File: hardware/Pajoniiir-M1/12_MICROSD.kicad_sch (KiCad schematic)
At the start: 23 parts

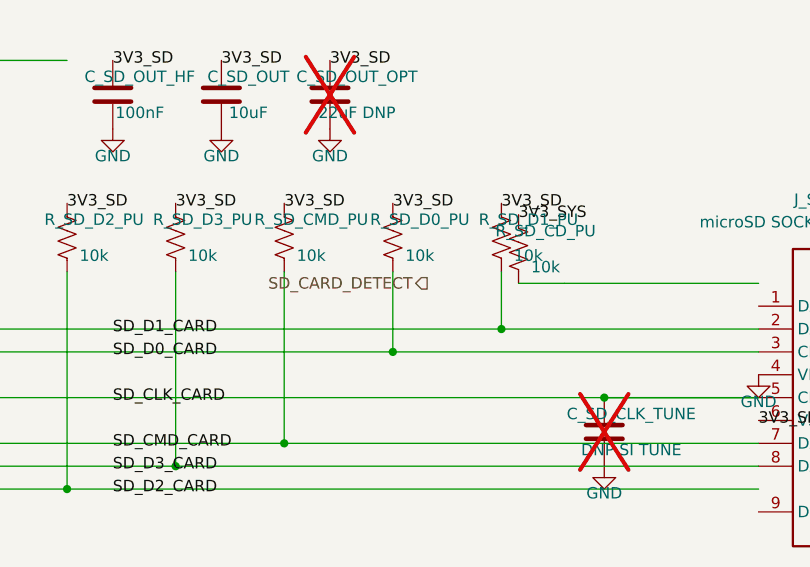
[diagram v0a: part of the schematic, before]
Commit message: hardware: bind remaining hierarchical ports to nets
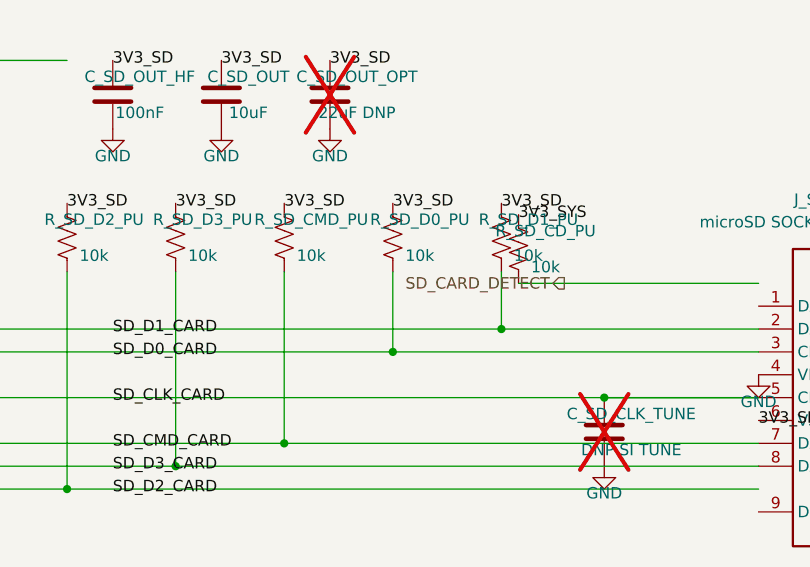
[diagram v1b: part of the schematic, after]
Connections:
- net SD_CARD_DETECT: now also R_SD_CD_PU.2
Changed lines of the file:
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@@
   )
   (wire (pts (xy 196.85 72.39) (xy 175.26 72.39)) (stroke (width 0) (type default)))
-  (hierarchical_label "SD_CARD_DETECT" (shape output) (at 160.02 72.39 180) (effects (font (size 1.27 1.27))))
+  (hierarchical_label "SD_CARD_DETECT" (shape output) (at 175.26 72.39 180) (effects (font (size 1.27 1.27))))
   (symbol
     (lib_id "Device:R_US") (at 170.18 68.58 0) (unit 1)

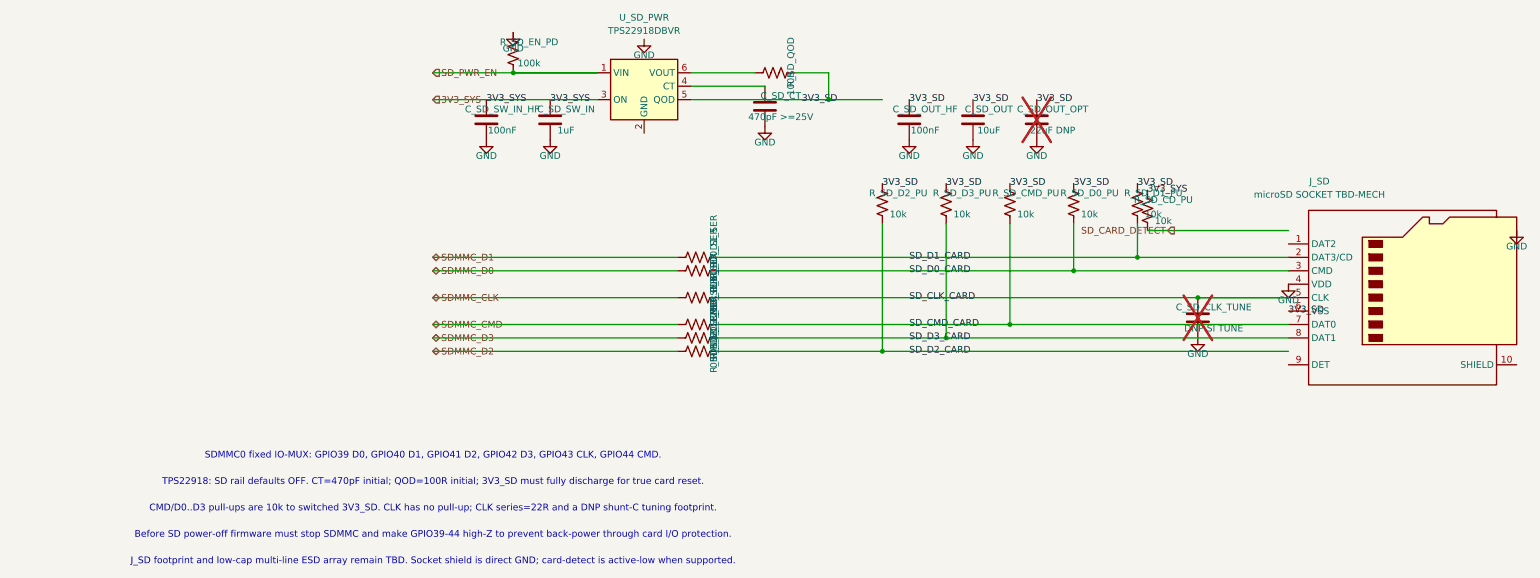
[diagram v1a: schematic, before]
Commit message: hardware: correct microSD power and signal mapping
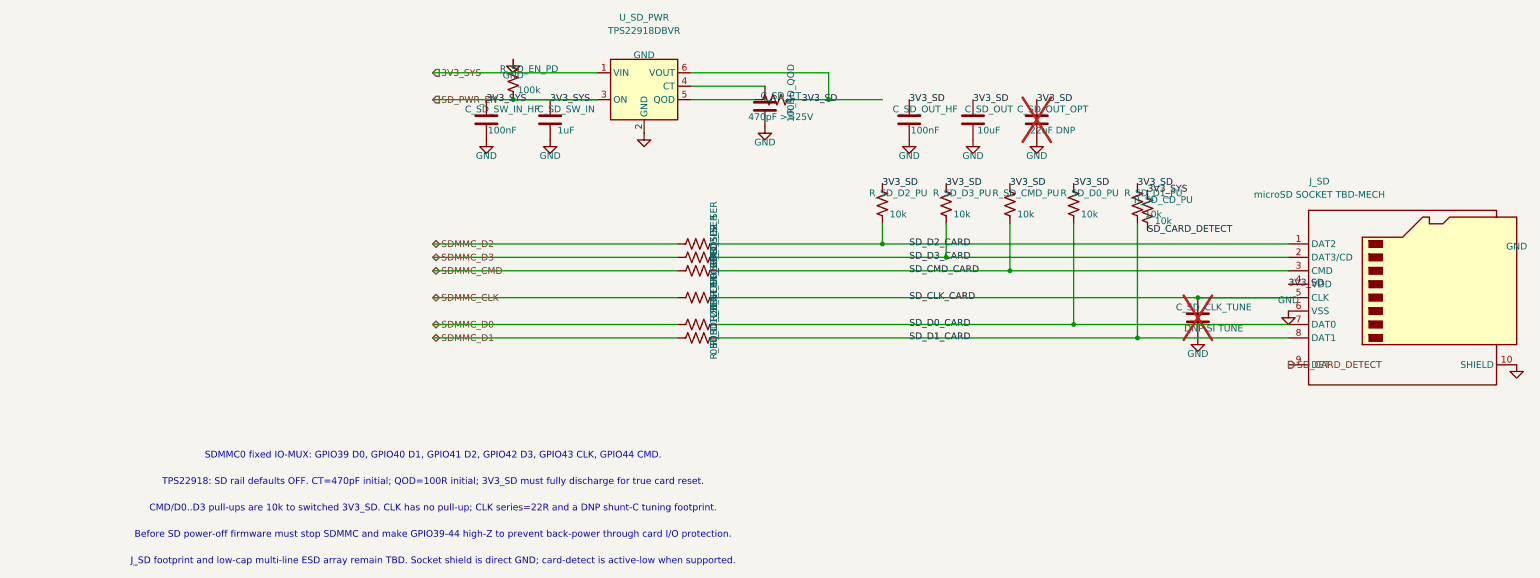
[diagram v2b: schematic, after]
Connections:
- net SD_PWR_EN is gone; now on net 3V3_SYS: R_SD_EN_PD.2, U_SD_PWR.1 (VIN)
- net 3V3_SD: now also J_SD.4 (VDD), U_SD_PWR.6 (VOUT); no longer J_SD.6 (VSS), U_SD_PWR.5 (QOD)
- net GND: now also J_SD.10 (SHIELD), J_SD.6 (VSS), U_SD_PWR.2 (GND); no longer J_SD.4 (VDD)
- net SD_CARD_DETECT: now also J_SD.9 (DET)
- net SD_CMD_CARD: now also J_SD.3 (CMD); no longer J_SD.7 (DAT0)
- net SD_D0_CARD: now also J_SD.7 (DAT0); no longer J_SD.3 (CMD)
- net SD_D1_CARD: now also J_SD.8 (DAT1); no longer J_SD.2 (DAT3/CD)
- net SD_D2_CARD: now also J_SD.1 (DAT2)
- net SD_D3_CARD: now also J_SD.2 (DAT3/CD); no longer J_SD.8 (DAT1)
- net at R_SD_QOD.1: now also U_SD_PWR.5 (QOD); no longer U_SD_PWR.6 (VOUT)
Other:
- moved on the sheet: R_SD_CMD_SER, R_SD_D0_SER, R_SD_D1_SER, R_SD_D2_SER, R_SD_D3_SER, R_SD_EN_PD, R_SD_QOD

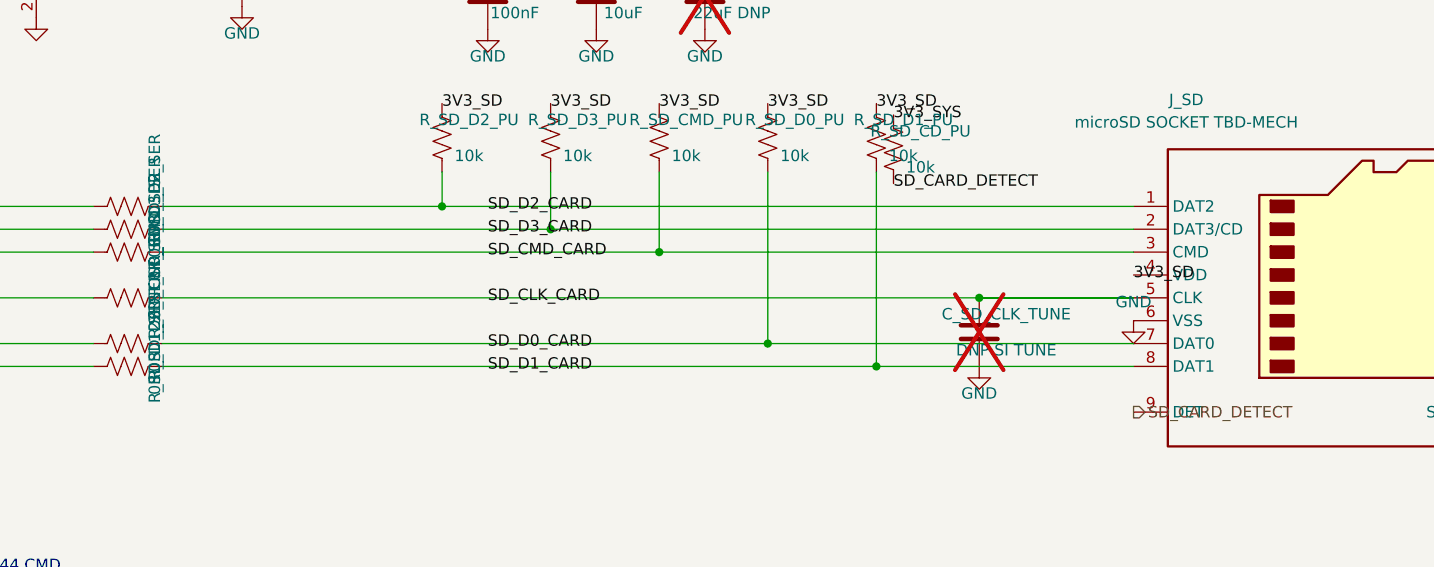
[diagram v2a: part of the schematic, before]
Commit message: hardware: close peripheral endpoint and net-alias gaps
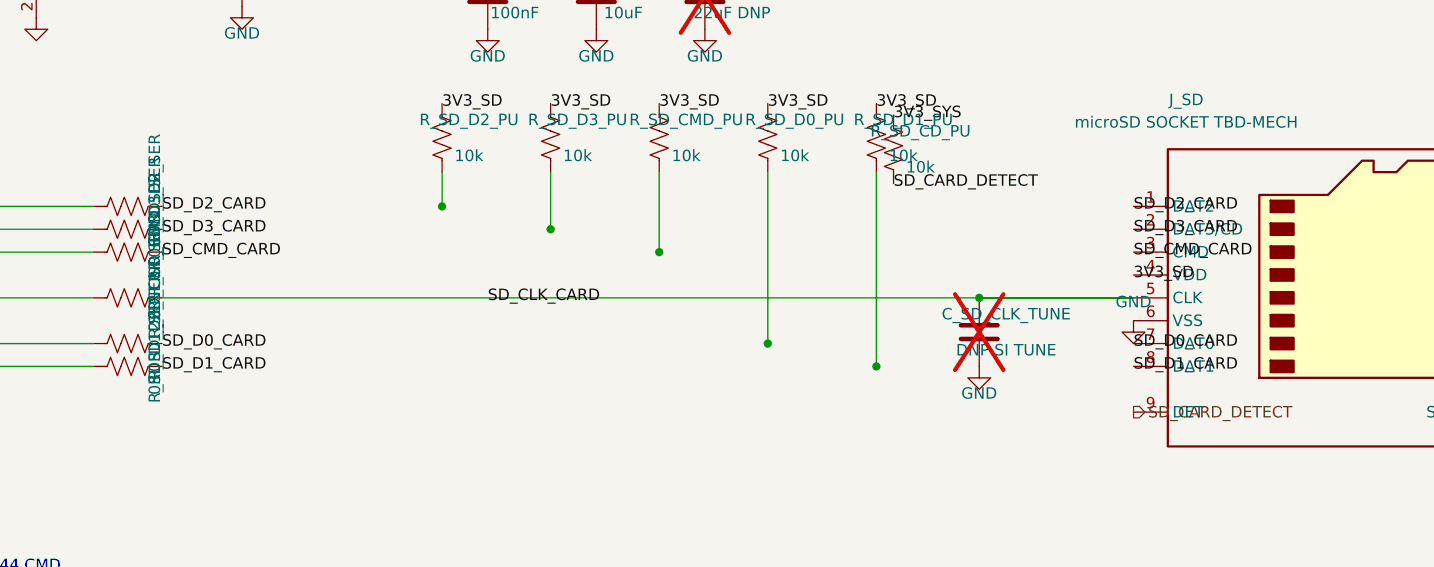
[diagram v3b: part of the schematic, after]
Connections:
- net SD_CMD_CARD: no longer R_SD_CMD_PU.2
- net SD_D0_CARD: no longer R_SD_D0_PU.2
- net SD_D1_CARD: no longer R_SD_D1_PU.2
- net SD_D2_CARD: no longer R_SD_D2_PU.2
- net SD_D3_CARD: no longer R_SD_D3_PU.2
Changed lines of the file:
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@@
     (comment 2 "Socket footprint and optional low-C ESD remain TBD-MECH/TBD-ESD")
   )
+  (label "SD_D2_CARD" (at 196.85 74.93 0) (effects (font (size 1.27 1.27))))
+  (label "SD_D3_CARD" (at 196.85 77.47 0) (effects (font (size 1.27 1.27))))
+  (label "SD_CMD_CARD" (at 196.85 80.01 0) (effects (font (size 1.27 1.27))))
+  (label "SD_D0_CARD" (at 196.85 90.17 0) (effects (font (size 1.27 1.27))))
+  (label "SD_D1_CARD" (at 196.85 92.71 0) (effects (font (size 1.27 1.27))))
   (label "SD_CARD_DETECT" (at 170.18 72.39 0) (effects (font (size 1.27 1.27))))
   (wire (pts (xy 83.82 42.545) (xy 109.855 42.545)) (stroke (width 0) (type default)))
@@
   )
   (wire (pts (xy 34.925 74.93) (xy 81.28 74.93)) (stroke (width 0) (type default)))
-  (wire (pts (xy 88.9 74.93) (xy 196.85 74.93)) (stroke (width 0) (type default)))
-  (label "SD_D2_CARD" (at 125.095 74.93 0) (effects (font (size 1.27 1.27))))
+  (label "SD_D2_CARD" (at 88.9 74.93 0) (effects (font (size 1.27 1.27))))
   (hierarchical_label "SDMMC_D3" (shape bidirectional) (at 34.925 77.47 0) (effects (font (size 1.27 1.27))))
   (symbol
@@
   )
   (wire (pts (xy 34.925 77.47) (xy 81.28 77.47)) (stroke (width 0) (type default)))
-  (wire (pts (xy 88.9 77.47) (xy 196.85 77.47)) (stroke (width 0) (type default)))
-  (label "SD_D3_CARD" (at 125.095 77.47 0) (effects (font (size 1.27 1.27))))
+  (label "SD_D3_CARD" (at 88.9 77.47 0) (effects (font (size 1.27 1.27))))
   (hierarchical_label "SDMMC_CMD" (shape bidirectional) (at 34.925 80.01 0) (effects (font (size 1.27 1.27))))
   (symbol
@@
   )
   (wire (pts (xy 34.925 80.01) (xy 81.28 80.01)) (stroke (width 0) (type default)))
-  (wire (pts (xy 88.9 80.01) (xy 196.85 80.01)) (stroke (width 0) (type default)))
-  (label "SD_CMD_CARD" (at 125.095 80.01 0) (effects (font (size 1.27 1.27))))
+  (label "SD_CMD_CARD" (at 88.9 80.01 0) (effects (font (size 1.27 1.27))))
   (hierarchical_label "SDMMC_CLK" (shape bidirectional) (at 34.925 85.09 0) (effects (font (size 1.27 1.27))))
   (symbol
@@
   )
   (wire (pts (xy 34.925 90.17) (xy 81.28 90.17)) (stroke (width 0) (type default)))
-  (wire (pts (xy 88.9 90.17) (xy 196.85 90.17)) (stroke (width 0) (type default)))
-  (label "SD_D0_CARD" (at 125.095 90.17 0) (effects (font (size 1.27 1.27))))
+  (label "SD_D0_CARD" (at 88.9 90.17 0) (effects (font (size 1.27 1.27))))
   (hierarchical_label "SDMMC_D1" (shape bidirectional) (at 34.925 92.71 0) (effects (font (size 1.27 1.27))))
   (symbol
@@
   )
   (wire (pts (xy 34.925 92.71) (xy 81.28 92.71)) (stroke (width 0) (type default)))
-  (wire (pts (xy 88.9 92.71) (xy 196.85 92.71)) (stroke (width 0) (type default)))
-  (label "SD_D1_CARD" (at 125.095 92.71 0) (effects (font (size 1.27 1.27))))
+  (label "SD_D1_CARD" (at 88.9 92.71 0) (effects (font (size 1.27 1.27))))
   (symbol
     (lib_id "Device:R_US") (at 120.015 67.31 0) (unit 1)

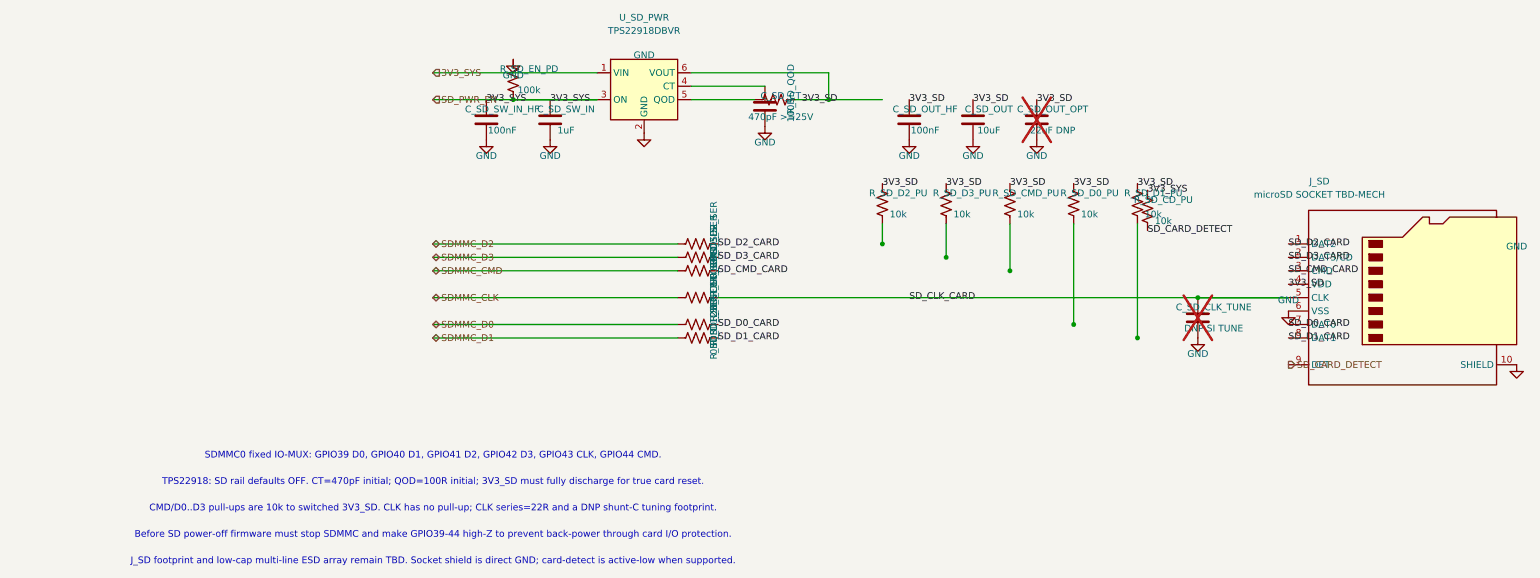
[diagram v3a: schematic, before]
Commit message: hardware: normalize endpoint nets and fix microSD input rail
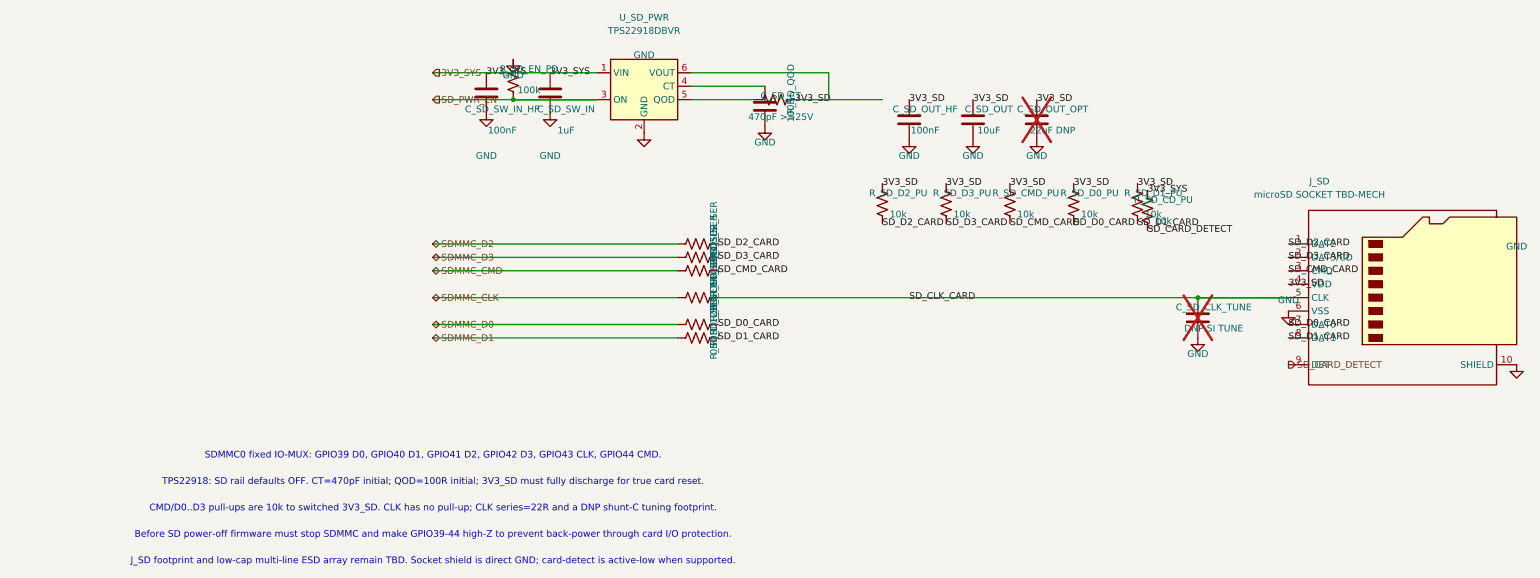
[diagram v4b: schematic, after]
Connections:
- net 3V3_SD: no longer U_SD_PWR.6 (VOUT)
- net 3V3_SYS: no longer R_SD_EN_PD.2, U_SD_PWR.3 (ON)
- net SD_CMD_CARD: now also R_SD_CMD_PU.2
- net SD_D0_CARD: now also R_SD_D0_PU.2
- net SD_D1_CARD: now also R_SD_D1_PU.2
- net SD_D2_CARD: now also R_SD_D2_PU.2
- net SD_D3_CARD: now also R_SD_D3_PU.2
- new net SD_PWR_EN: R_SD_EN_PD.2, U_SD_PWR.3 (ON)
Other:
- moved on the sheet: C_SD_SW_IN, C_SD_SW_IN_HF
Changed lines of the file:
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@@
   (wire (pts (xy 109.855 42.545) (xy 109.855 47.625)) (stroke (width 0) (type default)))
   (junction (at 50.165 47.625) (diameter 0) (color 0 0 0 0))
-  (junction (at 109.855 47.625) (diameter 0) (color 0 0 0 0))
-  (junction (at 120.015 74.93) (diameter 0) (color 0 0 0 0))
-  (junction (at 132.08 77.47) (diameter 0) (color 0 0 0 0))
-  (junction (at 144.145 80.01) (diameter 0) (color 0 0 0 0))
-  (junction (at 156.21 90.17) (diameter 0) (color 0 0 0 0))
-  (junction (at 168.275 92.71) (diameter 0) (color 0 0 0 0))
   (junction (at 179.705 85.09) (diameter 0) (color 0 0 0 0))
   (symbol
@@
   )
   (symbol
-    (lib_id "Device:C") (at 45.085 51.435 0) (unit 1)
+    (lib_id "Device:C") (at 45.085 46.355 0) (unit 1)
     (exclude_from_sim no) (in_bom yes) (on_board yes) (dnp no)
     (property "Reference" "C_SD_SW_IN_HF" (at 48.085 49.435 0) (effects (font (size 1.27 1.27))))
@@
     (instances (project "Pajoniiir-M1" (path "/2c8dd352-b7b8-4d9e-8f93-5dd43be2a100/3100000c-6b2a-4a3a-8c91-00000000000c" (reference "C_SD_SW_IN_HF") (unit 1))))
   )
-  (label "3V3_SYS" (at 45.085 47.625 0) (effects (font (size 1.27 1.27))))
-  (symbol
-    (lib_id "power:GND") (at 45.085 55.245 0) (unit 1)
+  (label "3V3_SYS" (at 45.085 42.545 0) (effects (font (size 1.27 1.27))))
+  (symbol
+    (lib_id "power:GND") (at 45.085 50.165 0) (unit 1)
     (exclude_from_sim no) (in_bom yes) (on_board yes) (dnp no)
     (property "Reference" "#PWR1245" (at 45.085 61.245 0) (effects (font (size 1.27 1.27)) (hide yes)))
@@
   )
   (symbol
-    (lib_id "Device:C") (at 57.15 51.435 0) (unit 1)
+    (lib_id "Device:C") (at 57.15 46.355 0) (unit 1)
     (exclude_from_sim no) (in_bom yes) (on_board yes) (dnp no)
     (property "Reference" "C_SD_SW_IN" (at 60.15 49.435 0) (effects (font (size 1.27 1.27))))
@@
     (instances (project "Pajoniiir-M1" (path "/2c8dd352-b7b8-4d9e-8f93-5dd43be2a100/3100000c-6b2a-4a3a-8c91-00000000000c" (reference "C_SD_SW_IN") (unit 1))))
   )
-  (label "3V3_SYS" (at 57.15 47.625 0) (effects (font (size 1.27 1.27))))
-  (symbol
-    (lib_id "power:GND") (at 57.15 55.245 0) (unit 1)
+  (label "3V3_SYS" (at 57.15 42.545 0) (effects (font (size 1.27 1.27))))
+  (symbol
+    (lib_id "power:GND") (at 57.15 50.165 0) (unit 1)
     (exclude_from_sim no) (in_bom yes) (on_board yes) (dnp no)
     (property "Reference" "#PWR1257" (at 57.15 61.245 0) (effects (font (size 1.27 1.27)) (hide yes)))
@@
     (instances (project "Pajoniiir-M1" (path "/2c8dd352-b7b8-4d9e-8f93-5dd43be2a100/3100000c-6b2a-4a3a-8c91-00000000000c" (reference "#PWR1203") (unit 1))))
   )
-  (wire (pts (xy 109.855 47.625) (xy 120.015 47.625)) (stroke (width 0) (type default)))
-  (label "3V3_SD" (at 104.775 47.625 0) (effects (font (size 1.27 1.27))))
+  (label "3V3_SD" (at 103.505 47.625 0) (effects (font (size 1.27 1.27))))
   (symbol
     (lib_id "Device:R_US") (at 99.695 47.625 90) (unit 1)
@@
   )
   (wire (pts (xy 83.82 47.625) (xy 95.885 47.625)) (stroke (width 0) (type default)))
-  (wire (pts (xy 103.505 47.625) (xy 109.855 47.625)) (stroke (width 0) (type default)))
+  (wire (pts (xy 103.505 47.625) (xy 120.015 47.625)) (stroke (width 0) (type default)))
   (symbol
     (lib_id "Device:C") (at 125.095 51.435 0) (unit 1)
@@
   )
   (label "3V3_SD" (at 120.015 63.5 0) (effects (font (size 1.27 1.27))))
-  (wire (pts (xy 120.015 71.12) (xy 120.015 74.93)) (stroke (width 0) (type default)))
+  (label "SD_D2_CARD" (at 120.015 71.12 0) (effects (font (size 1.27 1.27))))
   (symbol
     (lib_id "Device:R_US") (at 132.08 67.31 0) (unit 1)
@@
   )
   (label "3V3_SD" (at 132.08 63.5 0) (effects (font (size 1.27 1.27))))
-  (wire (pts (xy 132.08 71.12) (xy 132.08 77.47)) (stroke (width 0) (type default)))
+  (label "SD_D3_CARD" (at 132.08 71.12 0) (effects (font (size 1.27 1.27))))
   (symbol
     (lib_id "Device:R_US") (at 144.145 67.31 0) (unit 1)
@@
   )
   (label "3V3_SD" (at 144.145 63.5 0) (effects (font (size 1.27 1.27))))
-  (wire (pts (xy 144.145 71.12) (xy 144.145 80.01)) (stroke (width 0) (type default)))
+  (label "SD_CMD_CARD" (at 144.145 71.12 0) (effects (font (size 1.27 1.27))))
   (symbol
     (lib_id "Device:R_US") (at 156.21 67.31 0) (unit 1)
@@
   )
   (label "3V3_SD" (at 156.21 63.5 0) (effects (font (size 1.27 1.27))))
-  (wire (pts (xy 156.21 71.12) (xy 156.21 90.17)) (stroke (width 0) (type default)))
+  (label "SD_D0_CARD" (at 156.21 71.12 0) (effects (font (size 1.27 1.27))))
   (symbol
     (lib_id "Device:R_US") (at 168.275 67.31 0) (unit 1)
@@
   )
   (label "3V3_SD" (at 168.275 63.5 0) (effects (font (size 1.27 1.27))))
-  (wire (pts (xy 168.275 71.12) (xy 168.275 92.71)) (stroke (width 0) (type default)))
+  (label "SD_D1_CARD" (at 168.275 71.12 0) (effects (font (size 1.27 1.27))))
   (symbol
     (lib_id "Device:C") (at 179.705 88.9 0) (unit 1)
